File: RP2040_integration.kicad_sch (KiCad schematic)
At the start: 33 parts, among them J1 USB_B_Micro, J2 Conn_01x02, U1 NCP1117-3.3_SOT223, U2 W25Q128JVS, U3 RP2040, Y1 ABM8-272-T3

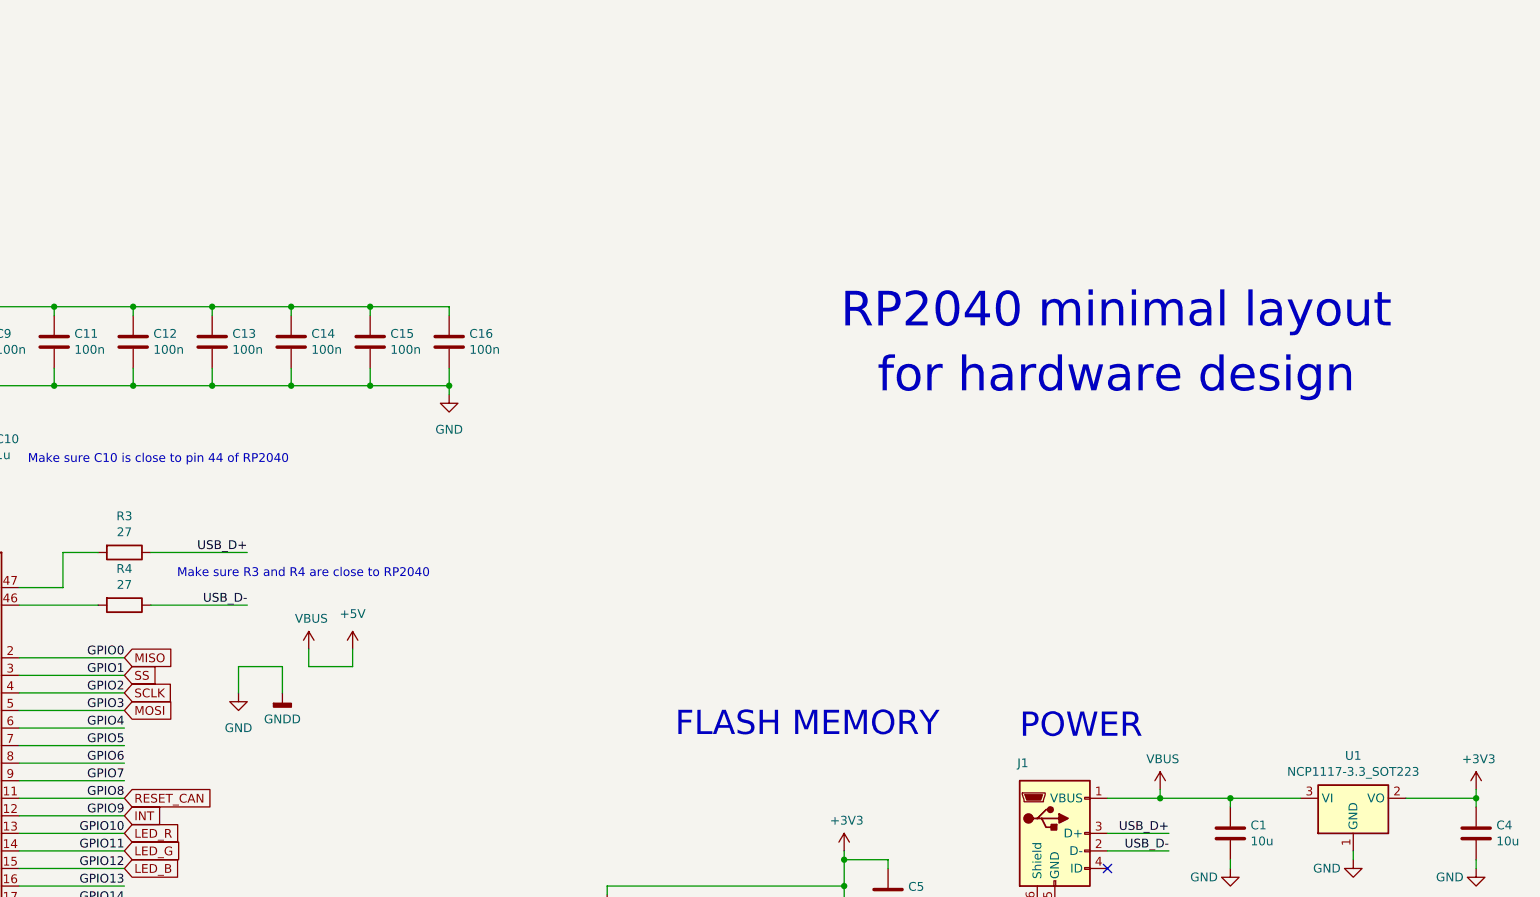
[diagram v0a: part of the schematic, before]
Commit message: Added all 3 ADC and routed them to RP2040 !
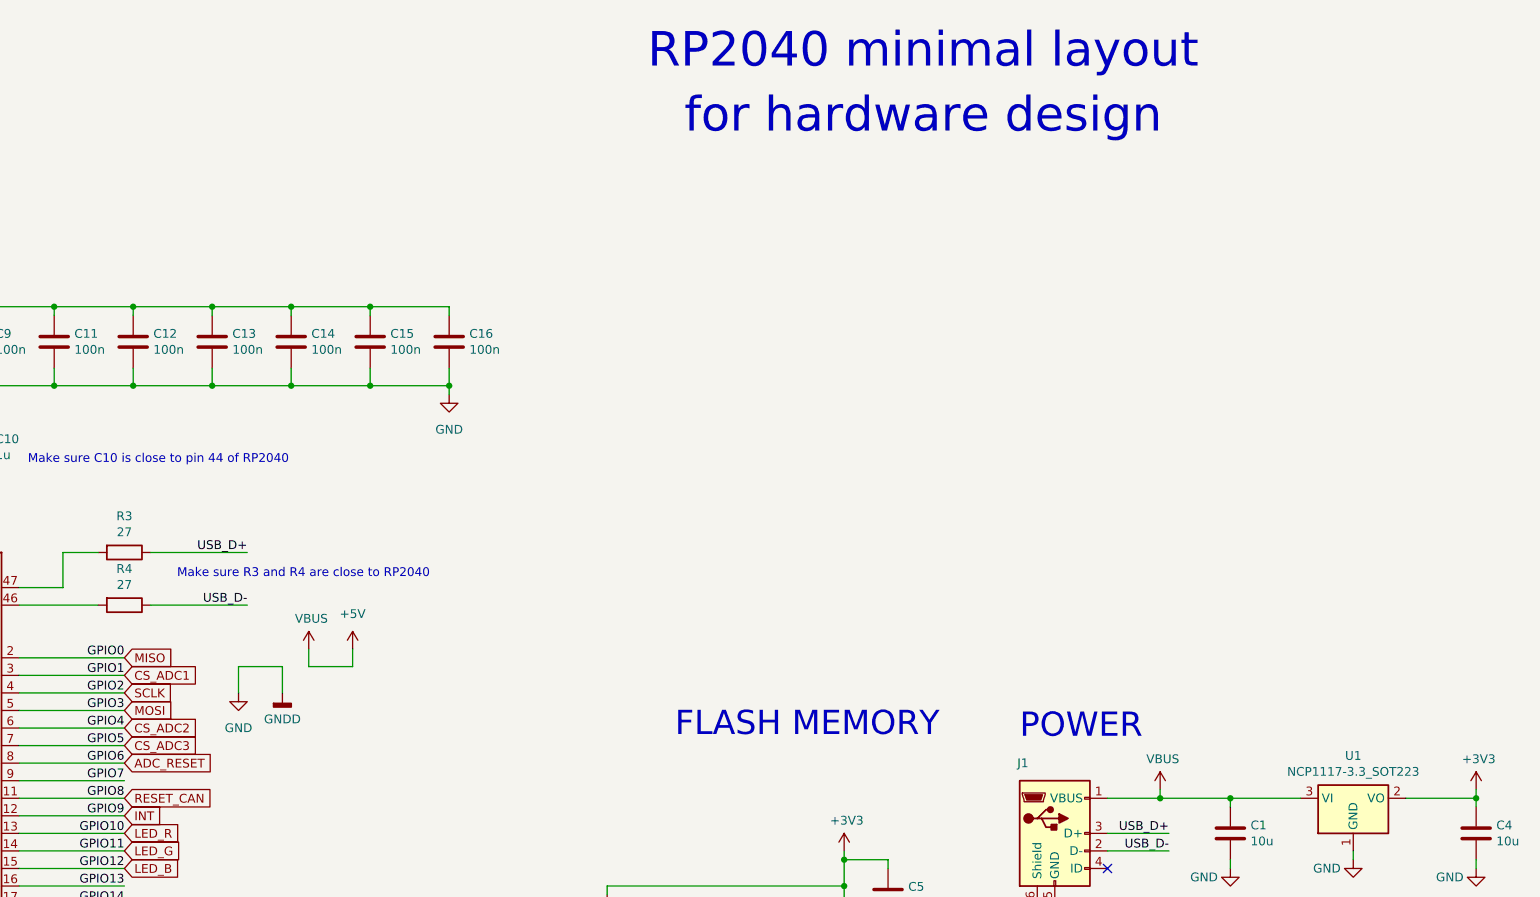
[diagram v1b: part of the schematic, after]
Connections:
- net GPIO4 renamed CS_ADC2
- net GPIO5 renamed CS_ADC3
- net GPIO6 renamed ADC_RESET
- net SS renamed CS_ADC1

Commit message: Schematic ok (je crois)
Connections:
- net GPIO16 renamed I2C_SDA
- net GPIO17 renamed I2C_SCL
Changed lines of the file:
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@@
 	(wire
 		(pts
-			(xy 132.08 162.56) (xy 147.32 162.56)
+			(xy 132.08 162.56) (xy 148.59 162.56)
 		)
 		(stroke
@@
 	(wire
 		(pts
-			(xy 132.08 160.02) (xy 147.32 160.02)
+			(xy 132.08 160.02) (xy 148.59 160.02)
 		)
 		(stroke
@@
 		)
 	)
+	(global_label "I2C_SCL"
+		(shape input)
+		(at 148.59 162.56 0)
+		(fields_autoplaced yes)
+		(effects
+			(font
+				(size 1.27 1.27)
+			)
+			(justify left)
+		)
+		(property "Intersheetrefs" "${INTERSHEET_REFS}"
+			(at 159.1347 162.56 0)
+			(effects
+				(font
+					(size 1.27 1.27)
+				)
+				(justify left)
+				(hide yes)
+			)
+		)
+	)
 	(global_label "INT"
 		(shape input)
@@
 			(effects
 				(font
+					(size 1.27 1.27)
+				)
+				(justify left)
+				(hide yes)
+			)
+		)
+	)
+	(global_label "I2C_SDA"
+		(shape input)
+		(at 148.59 160.02 0)
+		(fields_autoplaced yes)
+		(effects
+			(font
+				(size 1.27 1.27)
+			)
+			(justify left)
+		)
+		(property "Intersheetrefs" "${INTERSHEET_REFS}"
+			(at 159.1952 160.02 0)
+			(effects
+				(font

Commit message: Last Push pour que tu check, après je commence le Layout
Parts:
- added J15: SWD, Connector_PinHeader_2.54mm:PinHeader_1x04_P2.54mm_Vertical, symbol Connector:Conn_01x04_Pin
- added R21: 10k, Resistor_SMD:R_0603_1608Metric, symbol DPR_devices:R
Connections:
- net +3V3: now also J15.1 (Pin_1), R21.1
- net GND: now also J15.4 (Pin_4)
- net SWCLK: now also J15.2 (Pin_2)
- net SWD: now also J15.3 (Pin_3)
- net RUN: no longer names the net of U3.26 (RUN)
- net RUN: now also R21.2
- no-connect marks 1 -> 17
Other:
- note added: "SWD"

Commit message: Finito je te laisse check
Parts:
- R18, R20: value R_US -> 10k
- R19: value ? -> 10k
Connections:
- net GPIO18 renamed PWM_SERVO1
- net GPIO19 renamed PWM_SERVO2
- net GPIO20 renamed RESET
- no-connect marks 17 -> 14
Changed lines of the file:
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@@
 	)
 	(no_connect
-		(at 147.32 170.18)
-	)
-	(no_connect
 		(at 147.32 157.48)
 	)
@@
 	)
 	(no_connect
-		(at 147.32 165.1)
-	)
-	(no_connect
 		(at 147.32 137.16)
 	)
@@
 	)
 	(no_connect
-		(at 147.32 167.64)
-	)
-	(no_connect
 		(at 147.32 190.5)
 	)
@@
 	(wire
 		(pts
-			(xy 132.08 167.64) (xy 147.32 167.64)
+			(xy 132.08 167.64) (xy 148.59 167.64)
 		)
 		(stroke
@@
 	(wire
 		(pts
-			(xy 132.08 165.1) (xy 147.32 165.1)
+			(xy 132.08 165.1) (xy 148.59 165.1)
 		)
 		(stroke
@@
 	(wire
 		(pts
-			(xy 132.08 170.18) (xy 147.32 170.18)
+			(xy 132.08 170.18) (xy 148.59 170.18)
 		)
 		(stroke
@@
 		)
 	)
+	(global_label "PWM_SERVO1"
+		(shape input)
+		(at 148.59 165.1 0)
+		(fields_autoplaced yes)
+		(effects
+			(font
+				(size 1.27 1.27)
+			)
+			(justify left)
+		)
+		(property "Intersheetrefs" "${INTERSHEET_REFS}"
+			(at 163.9727 165.1 0)
+			(effects
+				(font
+					(size 1.27 1.27)
+				)
+				(justify left)
+				(hide yes)
+			)
+		)
+	)
 	(global_label "ADC_RESET"
 		(shape input)
@@
 		)
 	)
+	(global_label "RESET"
+		(shape input)
+		(at 148.59 170.18 0)
+		(fields_autoplaced yes)
+		(effects
+			(font
+				(size 1.27 1.27)
+			)
+			(justify left)
+		)
+		(property "Intersheetrefs" "${INTERSHEET_REFS}"
+			(at 157.3203 170.18 0)
+			(effects
+				(font
+					(size 1.27 1.27)
+				)
+				(justify left)
+				(hide yes)
+			)
+		)
+	)
 	(global_label "I2C_SCL"
 		(shape input)
@@
 		)
 	)
+	(global_label "PWM_SERVO2"
+		(shape input)
+		(at 148.59 167.64 0)
+		(fields_autoplaced yes)
+		(effects
+			(font
+				(size 1.27 1.27)
+			)
+			(justify left)
+		)
+		(property "Intersheetrefs" "${INTERSHEET_REFS}"
+			(at 163.9727 167.64 0)
+			(effects
+				(font
+					(size 1.27 1.27)
+				)
+				(justify left)
+				(hide yes)
+			)
+		)
+	)
 	(global_label "LED_B"
 		(shape input)
@@
 			)
 			(stroke
-				(width 0.254)
+				(width 0.7)
 				(type solid)
-				(color 0 0 132 1)
+				(color 0 0 255 1)
 			)
 			(fill
@@
 			)
 		)
-		(property "Description" ""
+		(property "Description" "USB Micro Type B connector"
 			(at 281.94 144.78 0)
 			(effects
@@
 					(size 1.27 1.27)
 				)
+				(hide yes)
 			)
 		)
@@
 			)
 		)
-		(property "Value" "R_US"
+		(property "Value" "10k"
 			(at 210.82 224.79 90)
 			(effects
@@
 			)
 		)
-		(property "Value" "?"
+		(property "Value" "10k"
 			(at 210.82 215.646 90)
 			(effects
@@
 			)
 		)
-		(property "Value" "R_US"
+		(property "Value" "10k"
 			(at 210.82 219.71 90)
 			(effects

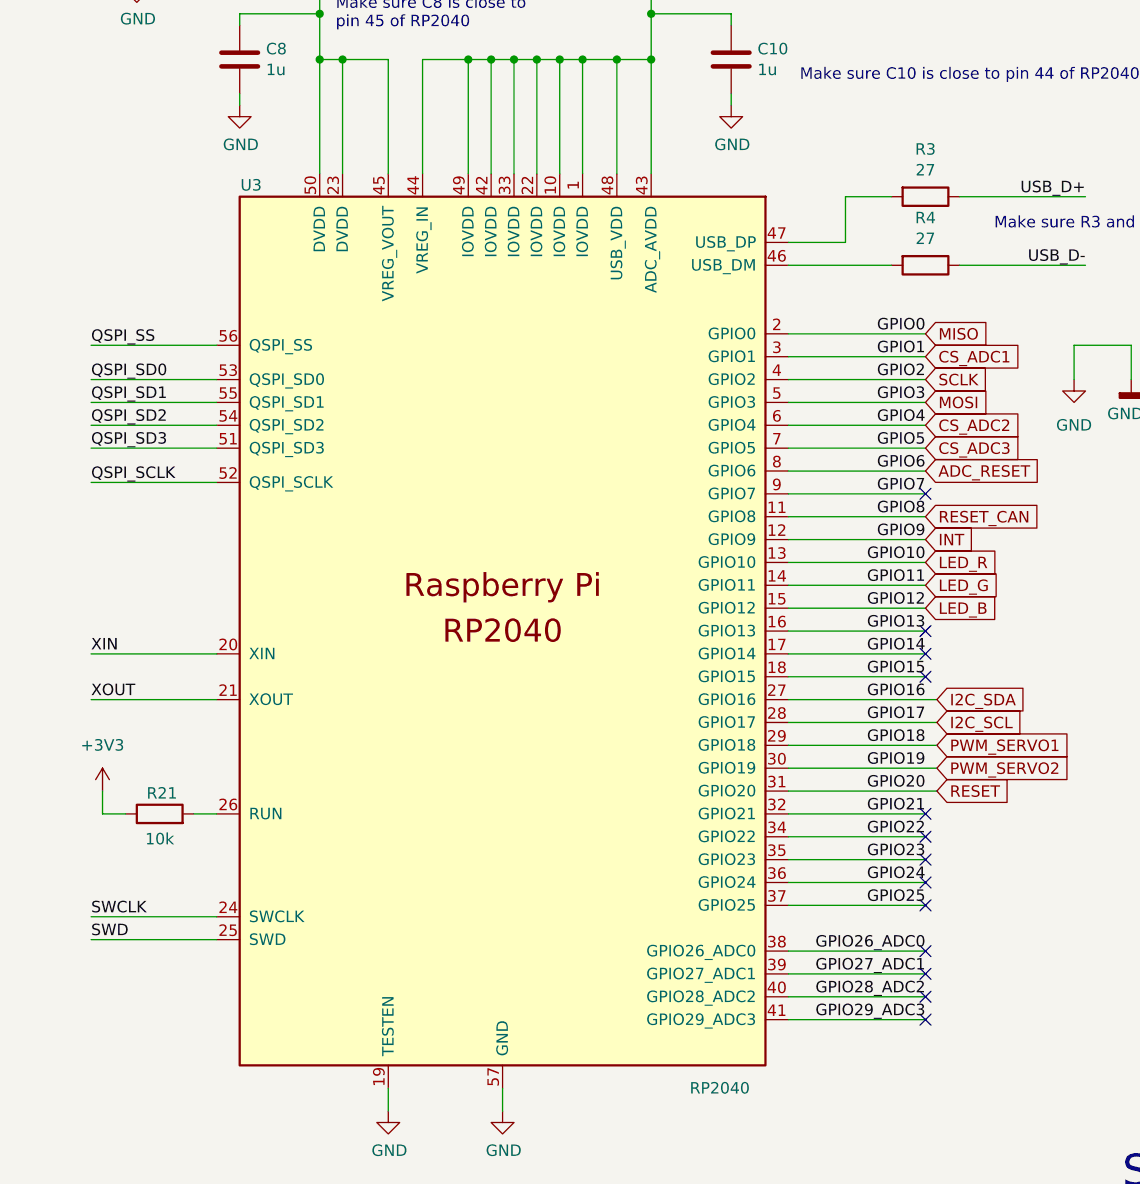
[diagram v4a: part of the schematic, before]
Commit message: added reset and bootsel buttons
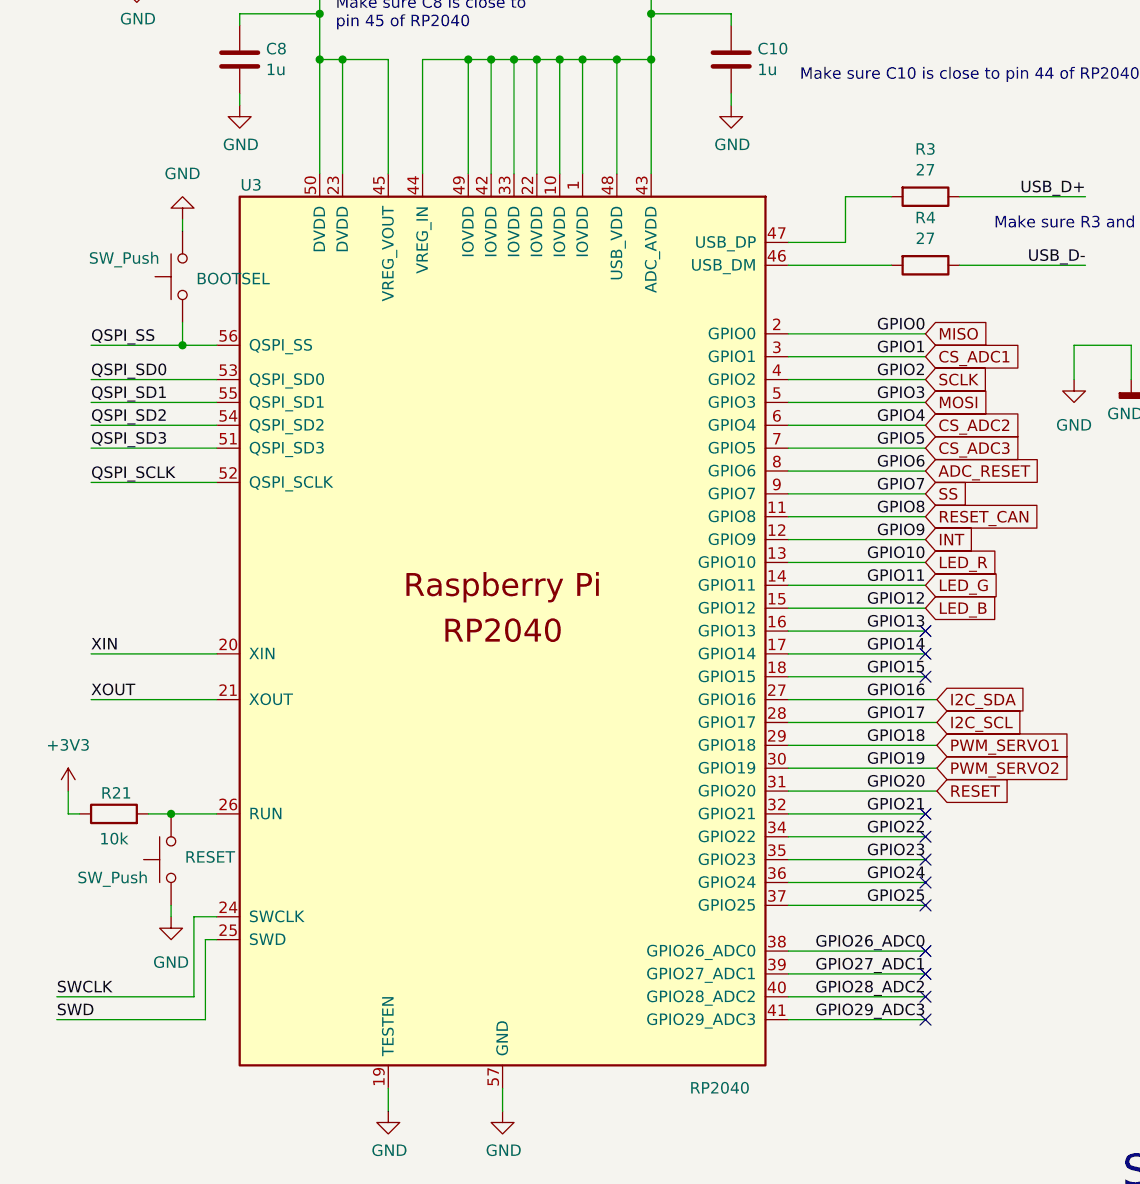
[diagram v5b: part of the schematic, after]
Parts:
- added BOOTSEL, RESET: SW_Push, Button_Switch_SMD:SW_SPST_B3U-1000P, symbol Switch:SW_Push
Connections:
- net GND: now also BOOTSEL.1, RESET.1
- net QSPI_SS: now also BOOTSEL.2
- net at R21.2, U3.26 (RUN): now also RESET.2
- net GPIO7 renamed SS
- no-connect marks 14 -> 13
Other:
- moved on the sheet: R21

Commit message: last modifications
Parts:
- renumbered BOOTSEL to BOOTSEL1, RESET to RESET1
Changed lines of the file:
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@@
 		(on_board yes)
 		(dnp no)
-		(property "Reference" "BOOTSEL"
+		(property "Reference" "BOOTSEL1"
 			(at 66.294 113.284 90)
 			(effects
@@
 			(project "Valvotron8000Pro"
 				(path "/e783bbdf-2a7f-40b9-9fb7-b62785862857/e081148b-fef9-4fa9-8f75-119abd10d809"
-					(reference "BOOTSEL")
+					(reference "BOOTSEL1")
 					(unit 1)
 				)
@@
 		(on_board yes)
 		(dnp no)
-		(property "Reference" "RESET"
+		(property "Reference" "RESET1"
 			(at 65.024 177.546 90)
 			(effects
@@
 			(project ""
 				(path "/e783bbdf-2a7f-40b9-9fb7-b62785862857/e081148b-fef9-4fa9-8f75-119abd10d809"
-					(reference "RESET")
-					(unit 1)
-				)
+					(reference "RESET1")
+					(unit 1)
+				)

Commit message: Dernières modifs
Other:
- moved on the sheet: J15
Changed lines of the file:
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@@
 	(text "SWD"
 		(exclude_from_sim no)
-		(at 262.636 212.09 0)
+		(at 262.636 207.01 0)
 		(effects
 			(font
@@
 	(wire
 		(pts
-			(xy 269.24 232.41) (xy 269.24 233.68)
+			(xy 269.24 227.33) (xy 269.24 228.6)
 		)
 		(stroke
@@
 	(wire
 		(pts
-			(xy 264.16 227.33) (xy 266.7 227.33)
+			(xy 264.16 222.25) (xy 266.7 222.25)
 		)
 		(stroke
@@
 	(wire
 		(pts
-			(xy 264.16 224.79) (xy 267.97 224.79)
+			(xy 264.16 219.71) (xy 267.97 219.71)
 		)
 		(stroke
@@
 	(wire
 		(pts
-			(xy 264.16 229.87) (xy 266.7 229.87)
+			(xy 264.16 224.79) (xy 266.7 224.79)
 		)
 		(stroke
@@
 	(wire
 		(pts
-			(xy 264.16 232.41) (xy 269.24 232.41)
+			(xy 264.16 227.33) (xy 269.24 227.33)
 		)
 		(stroke
@@
 	(wire
 		(pts
-			(xy 267.97 223.52) (xy 267.97 224.79)
+			(xy 267.97 218.44) (xy 267.97 219.71)
 		)
 		(stroke
@@
 	(global_label "SWD"
 		(shape input)
-		(at 266.7 229.87 0)
+		(at 266.7 224.79 0)
 		(fields_autoplaced yes)
 		(effects
@@
 		)
 		(property "Intersheetrefs" "${INTERSHEET_REFS}"
-			(at 273.6161 229.87 0)
+			(at 273.6161 224.79 0)
 			(effects
 				(font
@@
 	(global_label "SWCLK"
 		(shape input)
-		(at 266.7 227.33 0)
+		(at 266.7 222.25 0)
 		(fields_autoplaced yes)
 		(effects
@@
 		)
 		(property "Intersheetrefs" "${INTERSHEET_REFS}"
-			(at 275.9142 227.33 0)
+			(at 275.9142 222.25 0)
 			(effects
 				(font
@@
 		(polyline
 			(pts
-				(xy 248.92 214.63) (xy 276.86 214.63) (xy 278.13 215.9) (xy 278.13 238.76) (xy 276.86 240.03) (xy 252.73 240.03)
-				(xy 247.65 234.95) (xy 247.65 215.9)
+				(xy 248.92 209.55) (xy 276.86 209.55) (xy 278.13 210.82) (xy 278.13 233.68) (xy 276.86 234.95) (xy 252.73 234.95)
+				(xy 247.65 229.87) (xy 247.65 210.82)
 			)
 			(stroke
@@
 	(symbol
 		(lib_id "Connector:Conn_01x04_Pin")
-		(at 259.08 227.33 0)
+		(at 259.08 222.25 0)
 		(unit 1)
 		(exclude_from_sim no)
@@
 		(dnp no)
 		(property "Reference" "J15"
-			(at 254.508 226.568 0)
+			(at 254.508 221.488 0)
 			(effects
 				(font
@@
 		)
 		(property "Value" "SWD"
-			(at 254.762 229.108 0)
+			(at 254.762 224.028 0)
 			(effects
 				(font
@@
 		)
 		(property "Footprint" "Connector_PinHeader_2.54mm:PinHeader_1x04_P2.54mm_Vertical"
-			(at 259.08 227.33 0)
+			(at 259.08 222.25 0)
 			(effects
 				(font
@@
 		)
 		(property "Datasheet" "~"
-			(at 259.08 227.33 0)
+			(at 259.08 222.25 0)
 			(effects
 				(font
@@
 		)
 		(property "Description" "Generic connector, single row, 01x04, script generated"
-			(at 259.08 227.33 0)
+			(at 259.08 222.25 0)
 			(effects
 				(font
@@
 		(lib_name "+3V3_2")
 		(lib_id "power:+3V3")
-		(at 267.97 223.52 0)
+		(at 267.97 218.44 0)
 		(unit 1)
 		(exclude_from_sim no)
@@
 		(fields_autoplaced yes)
 		(property "Reference" "#PWR0103"
-			(at 267.97 227.33 0)
+			(at 267.97 222.25 0)
 			(effects
 				(font
@@
 		)
 		(property "Value" "+3V3"
-			(at 267.97 218.44 0)
+			(at 267.97 213.36 0)
 			(effects
 				(font
@@
 		)
 		(property "Footprint" ""
-			(at 267.97 223.52 0)
+			(at 267.97 218.44 0)
 			(effects
 				(font
@@
 		)
 		(property "Datasheet" ""
-			(at 267.97 223.52 0)
+			(at 267.97 218.44 0)
 			(effects
 				(font
@@
 		)
 		(property "Description" "Power symbol creates a global label with name \"+3V3\""
-			(at 267.97 223.52 0)
+			(at 267.97 218.44 0)
 			(effects
 				(font
@@
 	(symbol
 		(lib_id "DPR_devices:GND")
-		(at 269.24 233.68 0)
+		(at 269.24 228.6 0)
 		(unit 1)
 		(exclude_from_sim no)
@@
 		(fields_autoplaced yes)
 		(property "Reference" "#PWR0104"
-			(at 269.24 240.03 0)
+			(at 269.24 234.95 0)
 			(effects
 				(font
@@
 		)
 		(property "Value" "GND"
-			(at 269.24 238.76 0)
+			(at 269.24 233.68 0)
 			(effects
 				(font
@@
 		)
 		(property "Footprint" ""
-			(at 269.24 233.68 0)
+			(at 269.24 228.6 0)
 			(effects
 				(font
@@
 		)
 		(property "Datasheet" ""
-			(at 269.24 233.68 0)
+			(at 269.24 228.6 0)
 			(effects
 				(font
@@
 		)
 		(property "Description" "Power symbol creates a global label with name \"GND\" , ground"
-			(at 269.24 233.68 0)
+			(at 269.24 228.6 0)
 			(effects
 				(font
